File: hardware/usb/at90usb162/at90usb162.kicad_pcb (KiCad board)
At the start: 2 copper layers, 47.5 x 34.8 mm, 13 parts, among them IC1 AT90USB162-A, J1 USERPORT, P1 USB, SW1 DIPSW2, X1 8Mhz

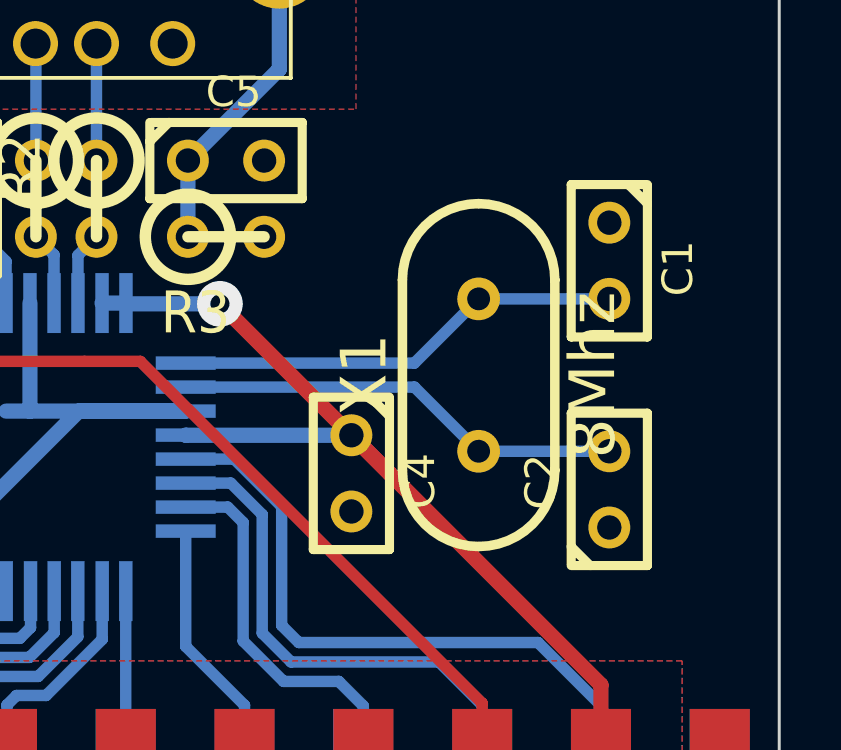
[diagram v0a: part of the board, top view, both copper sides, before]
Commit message: Hardware: Moved crystal to avoid possible short between oscillator case and VCC trace
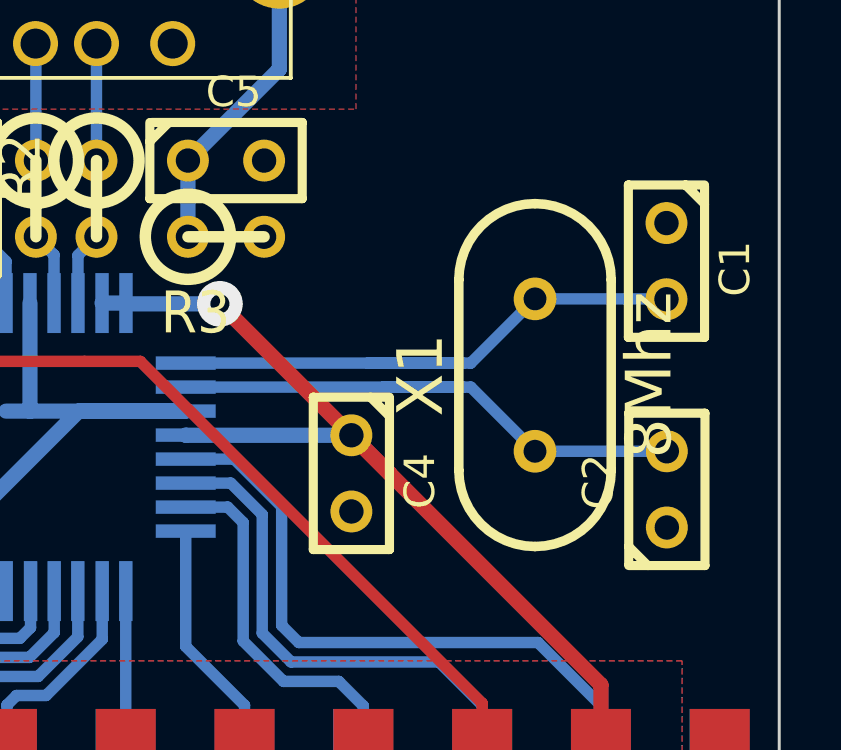
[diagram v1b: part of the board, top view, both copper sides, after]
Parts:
- moved C2 1.92 mm to (230.4, 142.3)
- moved C1 1.91 mm to (230.4, 134.7)
- moved X1 1.88 mm to (226.0, 138.5)
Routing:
- net N-0000014: track 15.0 -> 21.2 mm
- net N-0000013: track 15.0 -> 19.9 mm
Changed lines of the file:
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@@
     (thickness 1.6)
     (drawings 35)
-    (tracks 102)
+    (tracks 111)
     (zones 0)
     (modules 13)
@@
   )
   (module HC-49V (layer F.Cu)
-    (at 224.1042 138.5316 90)
+    (at 225.9838 138.5316 90)
     (descr "Quartz boitier HC-49 Vertical")
     (tags "QUARTZ DEV")
@@
   )
   (module C1 (layer F.Cu)
-    (at 228.4603 134.7216 270)
+    (at 230.3653 134.7343 270)
     (descr "Condensateur e = 1 pas")
     (tags C)
@@
   )
   (module C1 (layer F.Cu)
-    (at 228.4603 142.3416 90)
+    (at 230.378 142.3416 90)
     (descr "Condensateur e = 1 pas")
     (tags C)
@@
   (segment (start 209.169 146.9517) (end 208.8134 147.3073) (width 0.381) (layer B.Cu) (net 12))
   (segment (start 210.9597 138.0744) (end 206.7052 138.0744) (width 0.381) (layer F.Cu) (net 13))
-  (segment (start 204.7621 136.1313) (end 206.75092 136.1313) (width 0.381) (layer B.Cu) (net 13) (status 800000))
+  (segment (start 204.7621 136.1313) (end 206.75092 136.1313) (width 0.381) (layer B.Cu) (net 13))
   (via (at 204.7621 136.1313) (size 1.524) (layers F.Cu B.Cu) (net 13))
   (segment (start 206.7052 138.0744) (end 204.7621 136.1313) (width 0.381) (layer F.Cu) (net 13))
@@
   (segment (start 208.35112 139.73302) (end 209.1436 139.73302) (width 0.508) (layer B.Cu) (net 16))
   (segment (start 209.1436 139.73302) (end 214.34044 139.73302) (width 0.508) (layer B.Cu) (net 16))
-  (segment (start 228.4603 141.0716) (end 224.1042 141.0716) (width 0.381) (layer B.Cu) (net 17))
-  (segment (start 214.34044 138.93292) (end 221.96552 138.93292) (width 0.381) (layer B.Cu) (net 17))
-  (segment (start 221.96552 138.93292) (end 224.1042 141.0716) (width 0.381) (layer B.Cu) (net 17))
-  (segment (start 228.4603 135.9916) (end 224.1042 135.9916) (width 0.381) (layer B.Cu) (net 18))
-  (segment (start 214.34044 138.13282) (end 221.96298 138.13282) (width 0.381) (layer B.Cu) (net 18))
-  (segment (start 221.96298 138.13282) (end 224.1042 135.9916) (width 0.381) (layer B.Cu) (net 18))
+  (segment (start 225.9838 141.0716) (end 230.378 141.0716) (width 0.381) (layer B.Cu) (net 17))
+  (segment (start 221.6658 138.93292) (end 223.84512 138.93292) (width 0.381) (layer B.Cu) (net 17))
+  (segment (start 223.84512 138.93292) (end 225.9838 141.0716) (width 0.381) (layer B.Cu) (net 17))
+  (segment (start 220.9292 138.93292) (end 221.6658 138.93292) (width 0.381) (layer B.Cu) (net 17))
+  (segment (start 221.6658 138.93292) (end 223.59112 138.93292) (width 0.381) (layer B.Cu) (net 17))
+  (segment (start 214.34044 138.93292) (end 220.9292 138.93292) (width 0.381) (layer B.Cu) (net 17))
+  (segment (start 220.9292 138.93292) (end 221.96552 138.93292) (width 0.381) (layer B.Cu) (net 17))
+  (segment (start 225.9838 135.9916) (end 230.3526 135.9916) (width 0.381) (layer B.Cu) (net 18))
+  (segment (start 230.3526 135.9916) (end 230.3653 136.0043) (width 0.381) (layer B.Cu) (net 18))
+  (segment (start 220.4212 138.13282) (end 223.84258 138.13282) (width 0.381) (layer B.Cu) (net 18))
+  (segment (start 223.84258 138.13282) (end 225.9838 135.9916) (width 0.381) (layer B.Cu) (net 18))
+  (segment (start 220.853 138.13282) (end 223.58858 138.13282) (width 0.381) (layer B.Cu) (net 18))
+  (segment (start 214.34044 138.13282) (end 220.4212 138.13282) (width 0.381) (layer B.Cu) (net 18))
+  (segment (start 220.4212 138.13282) (end 220.853 138.13282) (width 0.381) (layer B.Cu) (net 18))
+  (segment (start 220.853 138.13282) (end 221.96298 138.13282) (width 0.381) (layer B.Cu) (net 18))
   (segment (start 210.74888 136.1313) (end 210.74888 134.53872) (width 0.381) (layer B.Cu) (net 19))
   (segment (start 210.74888 134.53872) (end 211.3661 133.9215) (width 0.381) (layer B.Cu) (net 19))

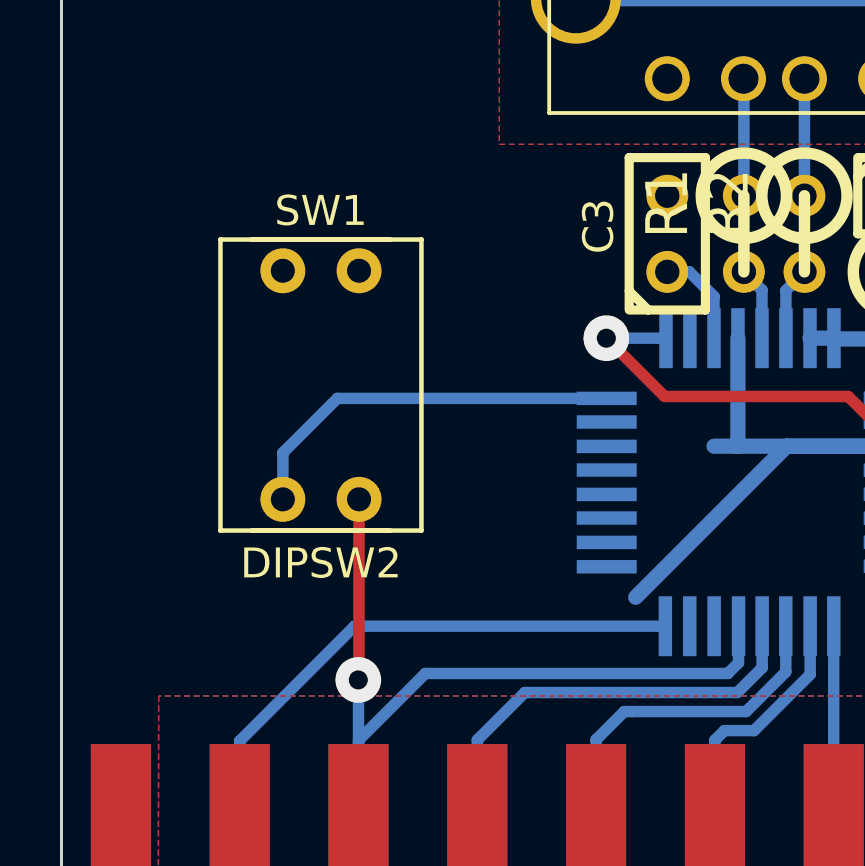
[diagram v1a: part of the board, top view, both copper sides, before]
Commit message: Hardware: Replaced dip-switch with simple pin header (use jumpers)
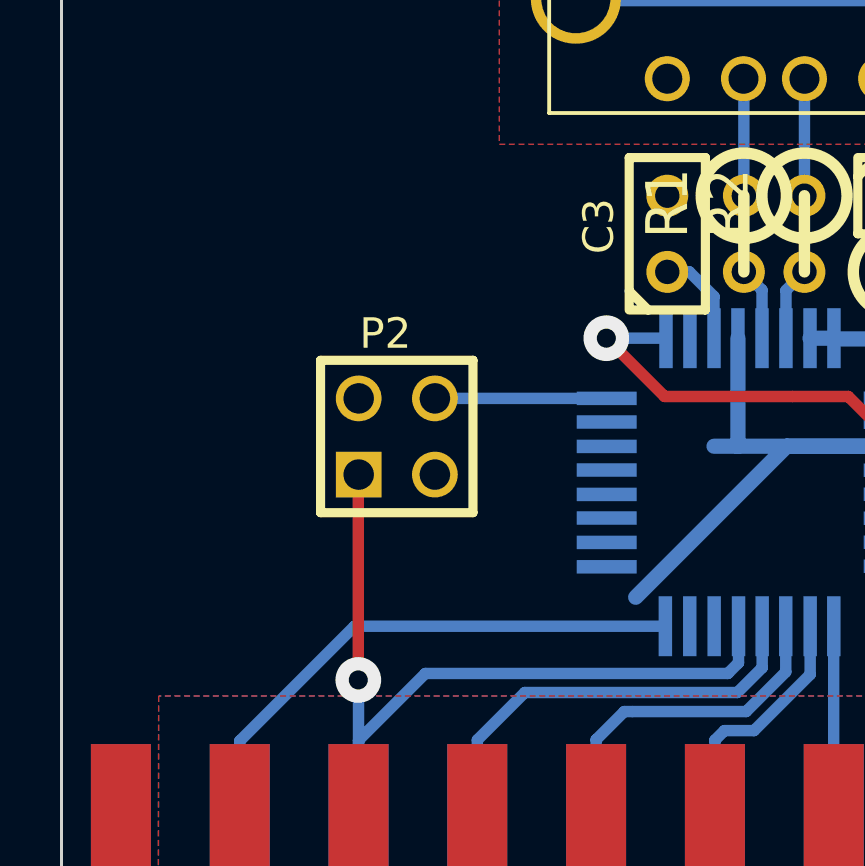
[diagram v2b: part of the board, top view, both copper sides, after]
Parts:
- removed SW1: DIPSW2, DIPSW2
- added P2: RESET, PIN_ARRAY_2X2, F.Cu at (197.8, 139.4)
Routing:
- net /ATRESET: track 13.1 -> 5.73 mm
- net /D7: track 28.3 -> 29.1 mm
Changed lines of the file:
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@@
     (area 178.563599 114.211099 255.5738 165.6537)
     (thickness 1.6)
-    (drawings 35)
-    (tracks 111)
+    (drawings 37)
+    (tracks 109)
     (zones 0)
     (modules 13)
@@
     )
   )
-  (module DIPSW2 (layer F.Cu)
-    (at 195.2498 137.6934)
-    (fp_text reference SW1 (at 0 -5.8) (layer F.SilkS)
-      (effects (font (size 1 1) (thickness 0.15)))
-    )
-    (fp_text value DIPSW2 (at 0 5.95) (layer F.SilkS)
-      (effects (font (size 1 1) (thickness 0.15)))
-    )
-    (fp_line (start -3.35 4.85) (end 3.35 4.85) (layer F.SilkS) (width 0.15))
-    (fp_line (start 3.35 4.85) (end 3.35 -4.85) (layer F.SilkS) (width 0.15))
-    (fp_line (start 3.35 -4.85) (end -3.35 -4.85) (layer F.SilkS) (width 0.15))
-    (fp_line (start -3.35 -4.85) (end -3.35 4.85) (layer F.SilkS) (width 0.15))
-    (fp_line (start -2.3 4.85) (end 2.3 4.85) (layer F.SilkS) (width 0.15))
-    (fp_line (start 2.3 -4.85) (end -2.3 -4.85) (layer F.SilkS) (width 0.15))
-    (pad 2 thru_hole circle (at -1.27 -3.81) (size 1.5 1.5) (drill 0.8)
-      (layers *.Cu *.Mask F.SilkS)
-      (net 16 GND)
-    )
-    (pad 4 thru_hole circle (at 1.27 -3.81) (size 1.5 1.5) (drill 0.8)
-      (layers *.Cu *.Mask F.SilkS)
-      (net 16 GND)
-    )
-    (pad 3 thru_hole circle (at 1.27 3.81) (size 1.5 1.5) (drill 0.8)
+  (module PIN_ARRAY_2X2 (layer F.Cu)
+    (at 197.7771 139.4079)
+    (descr "Double rangee de contacts 2 x 2 pins")
+    (tags CONN)
+    (fp_text reference P2 (at -0.381 -3.429) (layer F.SilkS)
+      (effects (font (size 1.016 1.016) (thickness 0.2032)))
+    )
+    (fp_text value RESET (at 0 3.048) (layer F.SilkS) hide
+      (effects (font (size 1.016 1.016) (thickness 0.2032)))
+    )
+    (fp_line (start -2.54 -2.54) (end 2.54 -2.54) (layer F.SilkS) (width 0.3048))
+    (fp_line (start 2.54 -2.54) (end 2.54 2.54) (layer F.SilkS) (width 0.3048))
+    (fp_line (start 2.54 2.54) (end -2.54 2.54) (layer F.SilkS) (width 0.3048))
+    (fp_line (start -2.54 2.54) (end -2.54 -2.54) (layer F.SilkS) (width 0.3048))
+    (pad 1 thru_hole rect (at -1.27 1.27) (size 1.524 1.524) (drill 1.016)
       (layers *.Cu *.Mask F.SilkS)
       (net 12 /D7)
     )
-    (pad 1 thru_hole circle (at -1.27 3.81) (size 1.5 1.5) (drill 0.8)
+    (pad 2 thru_hole circle (at -1.27 -1.27) (size 1.524 1.524) (drill 1.016)
+      (layers *.Cu *.Mask F.SilkS)
+      (net 16 GND)
+    )
+    (pad 3 thru_hole circle (at 1.27 1.27) (size 1.524 1.524) (drill 1.016)
+      (layers *.Cu *.Mask F.SilkS)
+      (net 16 GND)
+    )
+    (pad 4 thru_hole circle (at 1.27 -1.27) (size 1.524 1.524) (drill 1.016)
       (layers *.Cu *.Mask F.SilkS)
       (net 2 /ATRESET)
     )
-  )
+    (model pin_array/pins_array_2x2.wrl
+      (at (xyz 0 0 0))
+      (scale (xyz 1 1 1))
+      (rotate (xyz 0 0 0))
+    )
+  )
+  (gr_line (start 222.1738 138.5316) (end 189.992 138.5316) (angle 90) (layer Dwgs.User) (width 0.2))
+  (gr_line (start 196.4944 147.5105) (end 196.4944 141.9098) (angle 90) (layer Dwgs.User) (width 0.2))
   (gr_line (start 187.7949 132.6515) (end 187.7949 132.6261) (angle 90) (layer Dwgs.User) (width 0.2))
   (gr_line (start 224.0915 132.6515) (end 187.7949 132.6515) (angle 90) (layer Dwgs.User) (width 0.2))
@@
   (segment (start 196.3674 145.7325) (end 206.7306 145.7325) (width 0.381) (layer B.Cu) (net 1))
   (segment (start 192.5416 149.5583) (end 196.3674 145.7325) (width 0.381) (layer B.Cu) (net 1))
-  (segment (start 204.7748 138.1379) (end 195.7959 138.1379) (width 0.381) (layer B.Cu) (net 2))
-  (segment (start 193.9798 139.954) (end 193.9798 141.5034) (width 0.381) (layer B.Cu) (net 2))
-  (segment (start 195.7959 138.1379) (end 193.9798 139.954) (width 0.381) (layer B.Cu) (net 2))
+  (segment (start 204.7748 138.1379) (end 199.0471 138.1379) (width 0.381) (layer B.Cu) (net 2))
   (segment (start 209.3468 131.3815) (end 209.3468 127.4953) (width 0.381) (layer B.Cu) (net 3))
   (segment (start 209.3468 127.4953) (end 209.3341 127.4826) (width 0.381) (layer B.Cu) (net 3))
@@
   (segment (start 209.130898 147.942302) (end 209.9564 147.1168) (width 0.381) (layer B.Cu) (net 11))
   (segment (start 202.044298 147.942302) (end 209.130898 147.942302) (width 0.381) (layer B.Cu) (net 11))
+  (segment (start 196.4944 147.5232) (end 196.4944 140.6906) (width 0.381) (layer F.Cu) (net 12))
   (segment (start 196.5016 152.1611) (end 196.5016 147.5304) (width 0.381) (layer B.Cu) (net 12))
-  (segment (start 196.5198 147.4978) (end 196.5198 141.5034) (width 0.381) (layer F.Cu) (net 12))
-  (segment (start 196.4944 147.5232) (end 196.5198 147.4978) (width 0.381) (layer F.Cu) (net 12))
+  (segment (start 196.5016 147.5304) (end 196.4944 147.5232) (width 0.381) (layer B.Cu) (net 12))
   (via (at 196.4944 147.5232) (size 1.524) (layers F.Cu B.Cu) (net 12))
-  (segment (start 196.5016 147.5304) (end 196.4944 147.5232) (width 0.381) (layer B.Cu) (net 12))
+  (segment (start 196.4944 140.6906) (end 196.5071 140.6779) (width 0.381) (layer F.Cu) (net 12))
   (segment (start 196.5016 152.1611) (end 196.5016 149.5353) (width 0.381) (layer B.Cu) (net 12))
   (segment (start 196.5016 149.5353) (end 198.7296 147.3073) (width 0.381) (layer B.Cu) (net 12))
